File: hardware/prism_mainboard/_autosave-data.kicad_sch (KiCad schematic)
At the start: 2 parts, among them IC1 KTDM4G3C618BGIEAT, IC2 KTDM4G3C618BGIEAT

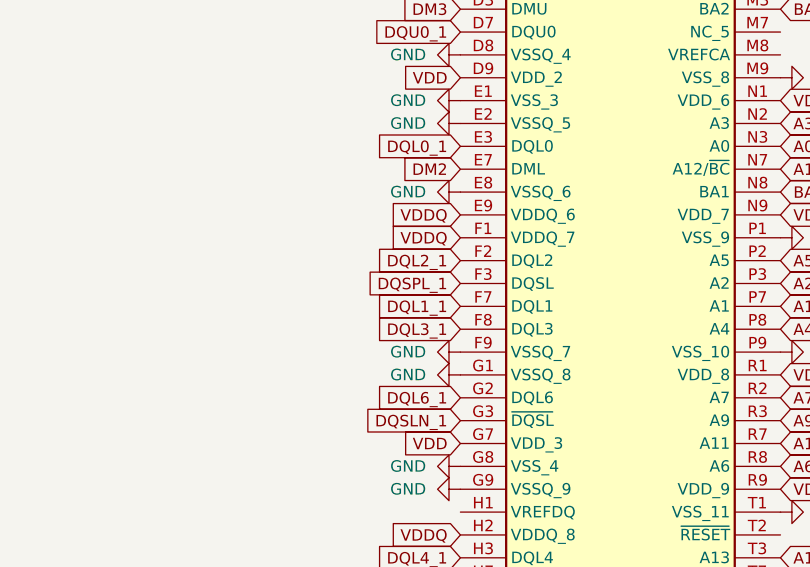
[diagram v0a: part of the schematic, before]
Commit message: Schematic Updates & PCB Population
Populated the PCB with footprints from Main PC, should show up now. Also been updating the KiCAD schematics to connect the DDR3L Modules to the FPGA. Should be done except for a few pins that I'm not sure what they do yet. But Addressing and data pins should be connected correctly now
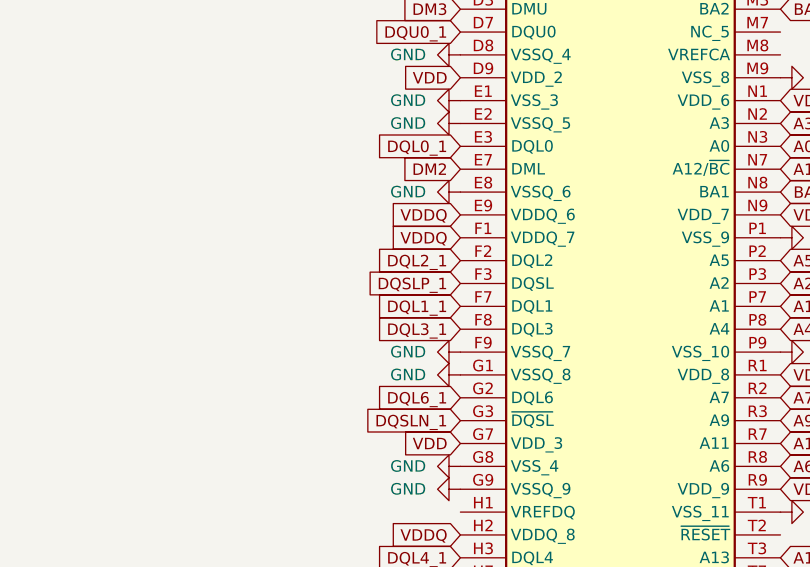
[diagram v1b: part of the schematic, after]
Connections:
- net DQSPL_1 renamed DQSLP_1
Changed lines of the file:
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@@
 		)
 	)
-	(global_label "DQSPL_1"
+	(global_label "DQSLP_1"
 		(shape input)
 		(at 166.37 114.3 180)
